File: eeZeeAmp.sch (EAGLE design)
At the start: 16 parts, among them IC1 LM386

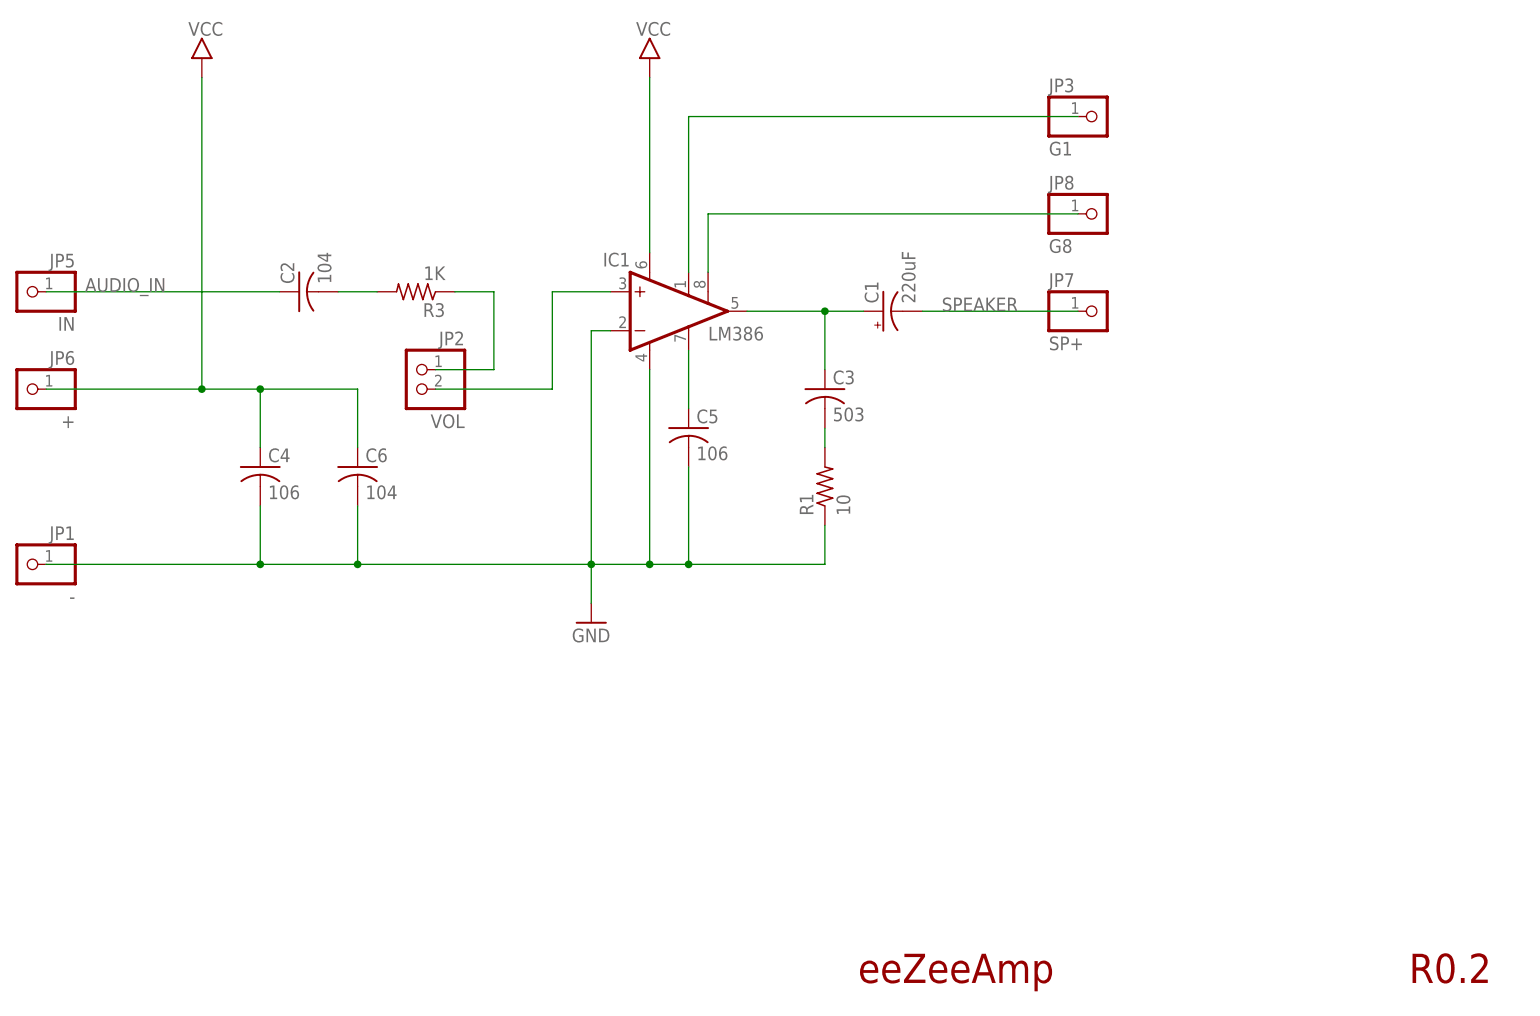
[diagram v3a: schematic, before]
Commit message: Separated variable resistor header into individual pins
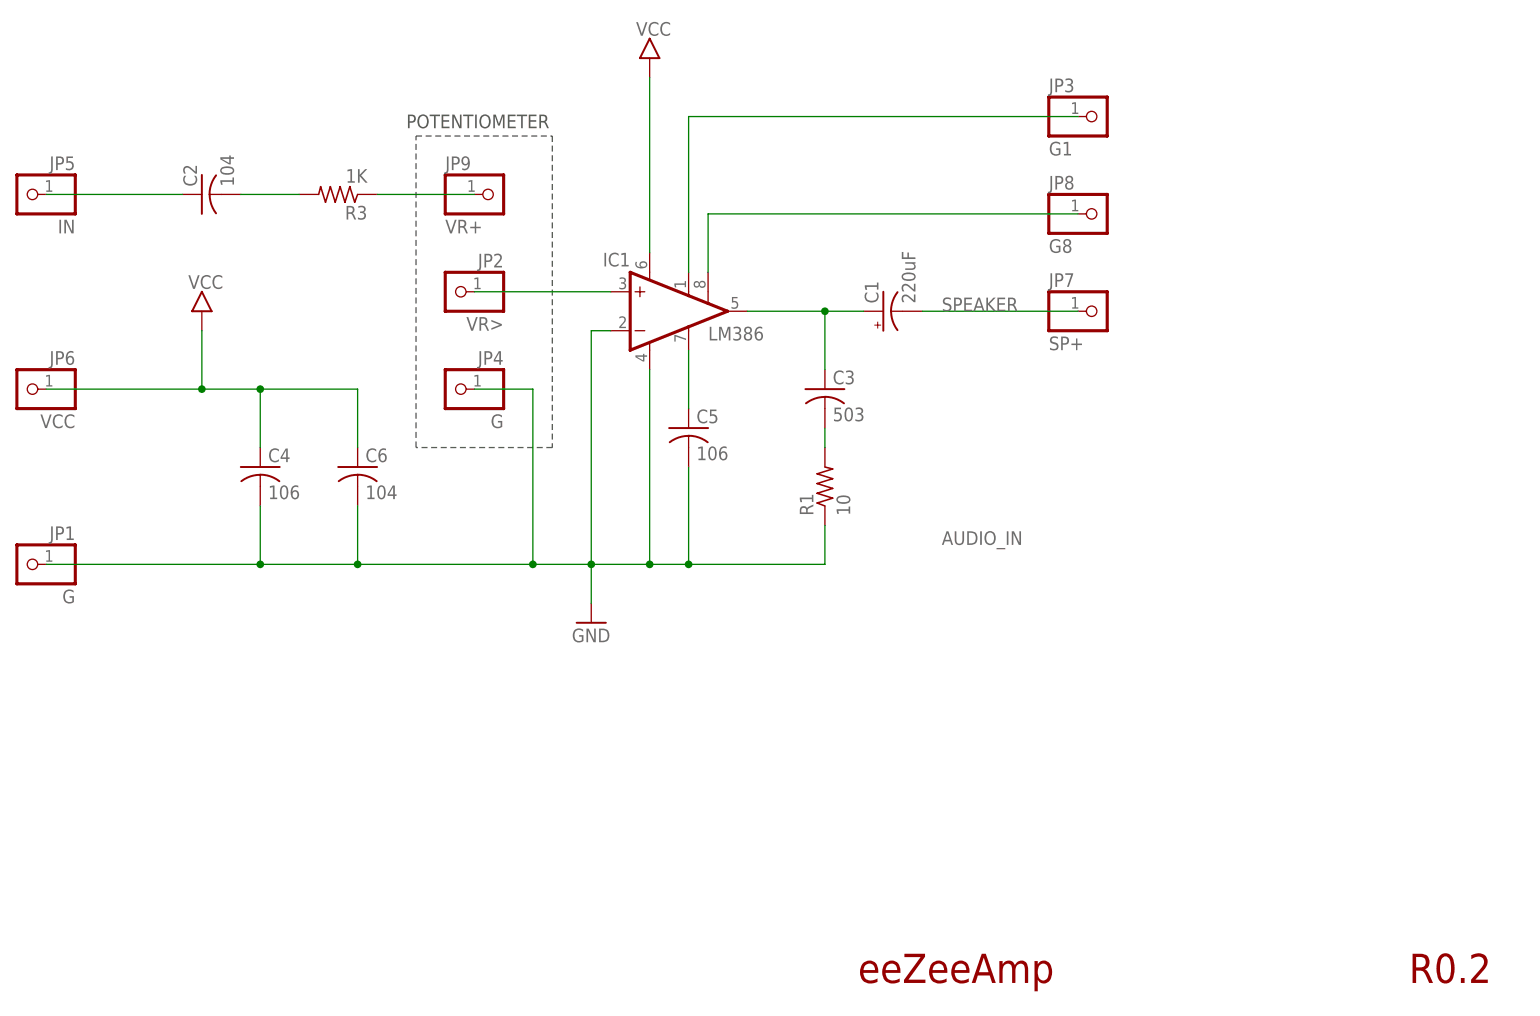
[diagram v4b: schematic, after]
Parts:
- added JP4: G, pinhead-2:PINHD-1X01_2.54-S
- added JP9: VR+, pinhead-2:PINHD-1X01_2.54-S
- JP1: value - -> G
- JP2: value VOL -> VR>; device pinhead-2:PINHD-1X02_2.54-S -> pinhead-2:PINHD-1X01_2.54-S
- JP6: value + -> VCC
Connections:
- net GND: now also JP4.1
- net N$1: now also JP2.1; no longer JP2.2
- net N$8: now also JP9.1; no longer JP2.1
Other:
- note added: "POTENTIOMETER"
- moved on the sheet: C2, JP5, R3
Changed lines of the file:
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@@
 <part name="C6" library="rcl" deviceset="C-US" device="C0603" value="104"/>
 <part name="JP5" library="pinhead-2" deviceset="PINHD-1X01" device="_2.54-S" value="IN"/>
-<part name="JP6" library="pinhead-2" deviceset="PINHD-1X01" device="_2.54-S" value="+"/>
+<part name="JP6" library="pinhead-2" deviceset="PINHD-1X01" device="_2.54-S" value="VCC"/>
 <part name="JP7" library="pinhead-2" deviceset="PINHD-1X01" device="_2.54-S" value="SP+"/>
-<part name="JP1" library="pinhead-2" deviceset="PINHD-1X01" device="_2.54-S" value="-"/>
-<part name="JP2" library="pinhead-2" deviceset="PINHD-1X02" device="_2.54-S" value="VOL"/>
+<part name="JP1" library="pinhead-2" deviceset="PINHD-1X01" device="_2.54-S" value="G"/>
 <part name="JP3" library="pinhead-2" deviceset="PINHD-1X01" device="_2.54-S" value="G1"/>
 <part name="JP8" library="pinhead-2" deviceset="PINHD-1X01" device="_2.54-S" value="G8"/>
+<part name="JP4" library="pinhead-2" deviceset="PINHD-1X01" device="_2.54-S" value="G"/>
+<part name="JP2" library="pinhead-2" deviceset="PINHD-1X01" device="_2.54-S" value="VR&gt;"/>
+<part name="JP9" library="pinhead-2" deviceset="PINHD-1X01" device="_2.54-S" value="VR+"/>
 </parts>
 <sheets>
@@
 <text x="159.258" y="24.13" size="3.81" layer="94">eeZeeAmp</text>
 <text x="231.14" y="24.13" size="3.81" layer="94">R0.2</text>
+<wire x1="101.6" y1="134.62" x2="119.38" y2="134.62" width="0.1524" layer="97" style="shortdash"/>
+<wire x1="119.38" y1="134.62" x2="119.38" y2="93.98" width="0.1524" layer="97" style="shortdash"/>
+<wire x1="119.38" y1="93.98" x2="101.6" y2="93.98" width="0.1524" layer="97" style="shortdash"/>
+<wire x1="101.6" y1="93.98" x2="101.6" y2="134.62" width="0.1524" layer="97" style="shortdash"/>
+<text x="100.33" y="135.636" size="1.778" layer="97">POTENTIOMETER</text>
 </plain>
 <instances>
 <instance part="IC1" gate="G$1" x="134.62" y="111.76"/>
 <instance part="C1" gate="G$1" x="162.56" y="111.76" rot="R90"/>
-<instance part="C2" gate="G$1" x="86.36" y="114.3" rot="R90"/>
+<instance part="C2" gate="G$1" x="73.66" y="127" rot="R90"/>
 <instance part="C3" gate="G$1" x="154.94" y="101.6"/>
 <instance part="R1" gate="G$1" x="154.94" y="88.9" rot="R90"/>
-<instance part="R3" gate="G$1" x="101.6" y="114.3" rot="R180"/>
+<instance part="R3" gate="G$1" x="91.44" y="127" rot="R180"/>
 <instance part="U$1" gate="G$1" x="132.08" y="142.24"/>
-<instance part="U$2" gate="G$1" x="73.66" y="142.24"/>
+<instance part="U$2" gate="G$1" x="73.66" y="109.22"/>
 <instance part="C4" gate="G$1" x="81.28" y="91.44"/>
 <instance part="GND1" gate="1" x="124.46" y="71.12"/>
@@
 <instance part="FRAME1" gate="G$2" x="147.32" y="2.54"/>
 <instance part="C6" gate="G$1" x="93.98" y="91.44"/>
-<instance part="JP5" gate="A" x="50.8" y="114.3" rot="MR0"/>
+<instance part="JP5" gate="A" x="50.8" y="127" rot="MR0"/>
 <instance part="JP6" gate="A" x="50.8" y="101.6" rot="MR0"/>
 <instance part="JP7" gate="A" x="190.5" y="111.76"/>
 <instance part="JP1" gate="A" x="50.8" y="78.74" rot="MR0"/>
-<instance part="JP2" gate="A" x="101.6" y="101.6" rot="MR0"/>
 <instance part="JP3" gate="A" x="190.5" y="137.16"/>
 <instance part="JP8" gate="A" x="190.5" y="124.46"/>
+<instance part="JP4" gate="A" x="106.68" y="101.6" rot="MR0"/>
+<instance part="JP2" gate="A" x="106.68" y="114.3" rot="MR0"/>
+<instance part="JP9" gate="A" x="111.76" y="127"/>
 </instances>
 <busses>
@@
 <segment>
 <pinref part="IC1" gate="G$1" pin="+IN"/>
-<wire x1="127" y1="114.3" x2="119.38" y2="114.3" width="0.1524" layer="91"/>
-<wire x1="119.38" y1="114.3" x2="119.38" y2="101.6" width="0.1524" layer="91"/>
-<wire x1="119.38" y1="101.6" x2="104.14" y2="101.6" width="0.1524" layer="91"/>
-<pinref part="JP2" gate="A" pin="2"/>
+<wire x1="127" y1="114.3" x2="109.22" y2="114.3" width="0.1524" layer="91"/>
+<pinref part="JP2" gate="A" pin="1"/>
 </segment>
 </net>
@@
 <segment>
 <pinref part="C2" gate="G$1" pin="2"/>
-<wire x1="91.44" y1="114.3" x2="96.52" y2="114.3" width="0.1524" layer="91"/>
+<wire x1="78.74" y1="127" x2="86.36" y2="127" width="0.1524" layer="91"/>
 <pinref part="R3" gate="G$1" pin="2"/>
 </segment>
@@
 <segment>
 <pinref part="R3" gate="G$1" pin="1"/>
-<wire x1="106.68" y1="114.3" x2="111.76" y2="114.3" width="0.1524" layer="91"/>
-<wire x1="104.14" y1="104.14" x2="111.76" y2="104.14" width="0.1524" layer="91"/>
-<wire x1="111.76" y1="104.14" x2="111.76" y2="114.3" width="0.1524" layer="91"/>
-<pinref part="JP2" gate="A" pin="1"/>
+<wire x1="109.22" y1="127" x2="96.52" y2="127" width="0.1524" layer="91"/>
+<pinref part="JP9" gate="A" pin="1"/>
 </segment>
 </net>
@@
 </segment>
 <segment>
-<wire x1="73.66" y1="101.6" x2="73.66" y2="142.24" width="0.1524" layer="91"/>
+<wire x1="73.66" y1="101.6" x2="73.66" y2="109.22" width="0.1524" layer="91"/>
 <pinref part="U$2" gate="G$1" pin="VCC"/>
 <wire x1="53.34" y1="101.6" x2="73.66" y2="101.6" width="0.1524" layer="91"/>
@@
 <segment>
 <pinref part="C2" gate="G$1" pin="1"/>
-<label x="58.42" y="114.3" size="1.778" layer="95"/>
-<wire x1="53.34" y1="114.3" x2="83.82" y2="114.3" width="0.1524" layer="91"/>
+<label x="170.18" y="81.28" size="1.778" layer="95"/>
+<wire x1="53.34" y1="127" x2="71.12" y2="127" width="0.1524" layer="91"/>
 <pinref part="JP5" gate="A" pin="1"/>
 </segment>
@@
 <pinref part="C4" gate="G$1" pin="2"/>
 <wire x1="81.28" y1="78.74" x2="93.98" y2="78.74" width="0.1524" layer="91"/>
-<wire x1="93.98" y1="78.74" x2="124.46" y2="78.74" width="0.1524" layer="91"/>
+<wire x1="93.98" y1="78.74" x2="116.84" y2="78.74" width="0.1524" layer="91"/>
+<wire x1="116.84" y1="78.74" x2="124.46" y2="78.74" width="0.1524" layer="91"/>
 <wire x1="81.28" y1="86.36" x2="81.28" y2="78.74" width="0.1524" layer="91"/>
 <junction x="81.28" y="78.74"/>
@@
 <junction x="93.98" y="78.74"/>
 <pinref part="JP1" gate="A" pin="1"/>
+<pinref part="JP4" gate="A" pin="1"/>
+<wire x1="109.22" y1="101.6" x2="116.84" y2="101.6" width="0.1524" layer="91"/>
+<wire x1="116.84" y1="101.6" x2="116.84" y2="78.74" width="0.1524" layer="91"/>
+<junction x="116.84" y="78.74"/>
 </segment>
 </net>
